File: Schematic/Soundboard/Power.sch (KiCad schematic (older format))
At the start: 34 parts, among them U1 STM32f429IIT6-units

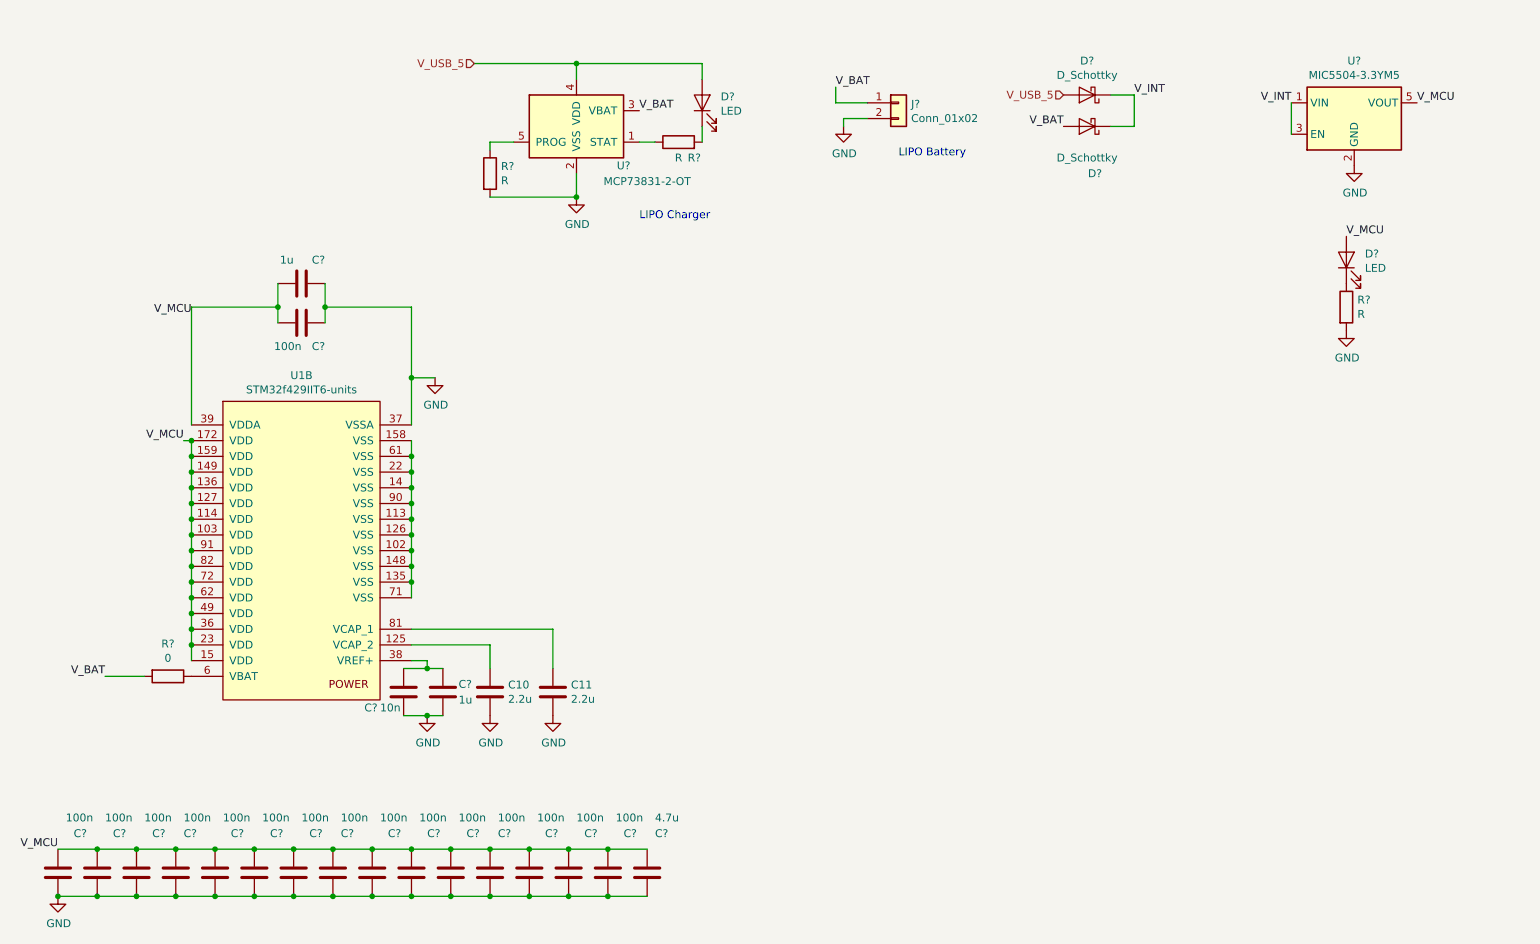
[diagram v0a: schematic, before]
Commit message: Complete part selection. Start connections
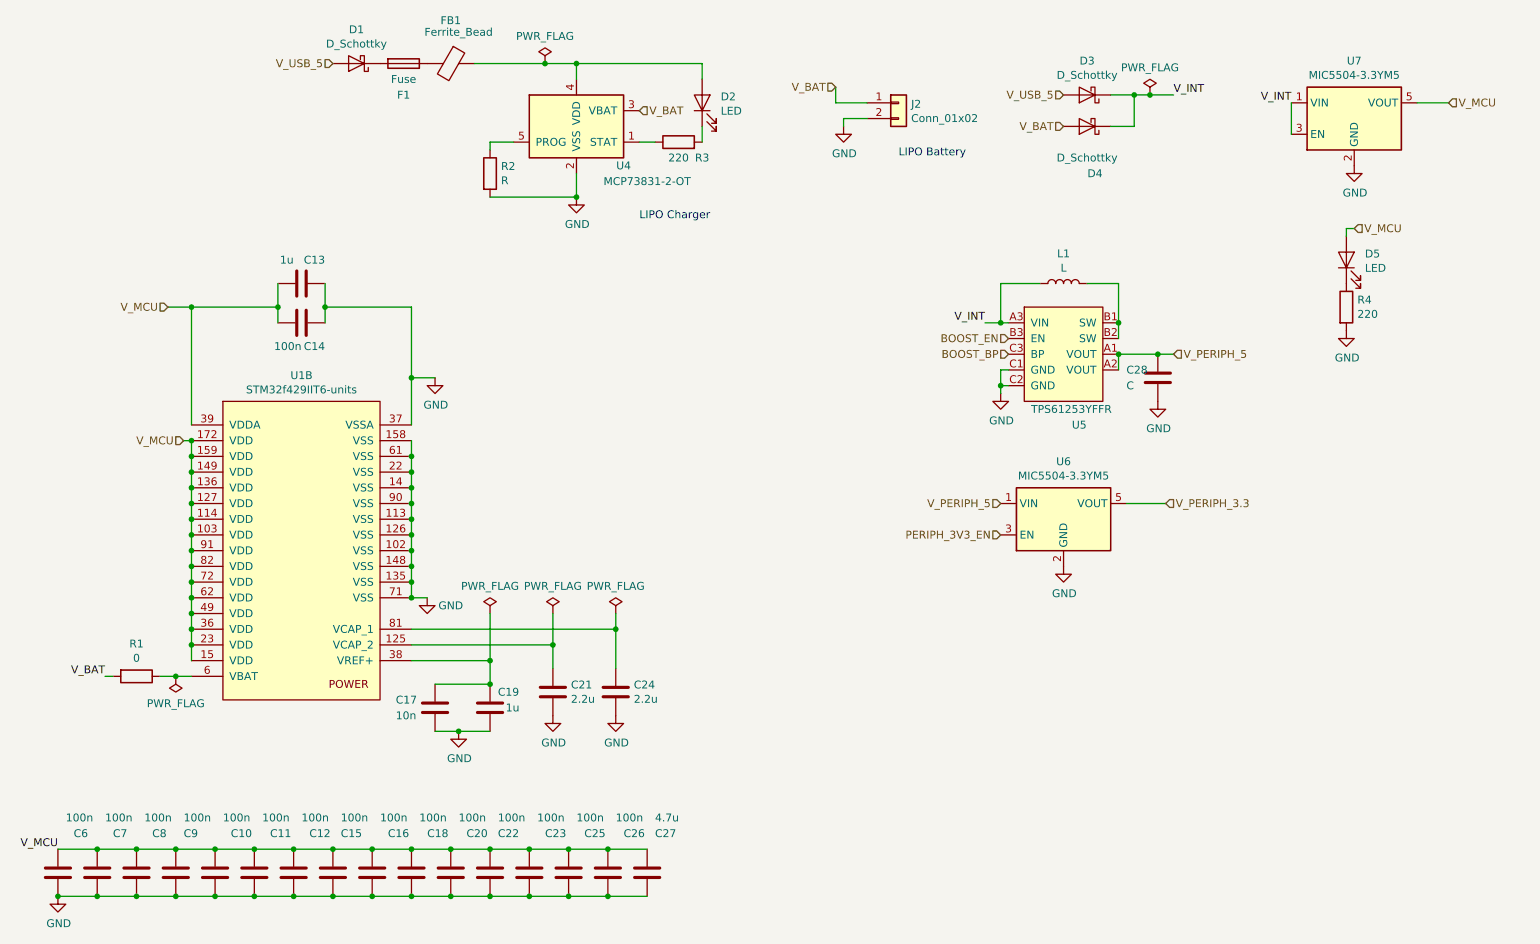
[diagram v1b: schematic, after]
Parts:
- added C28: C, Capacitor_SMD:C_0603_1608Metric_Pad1.05x0.95mm_HandSolder, symbol Device:C
- added D1: D_Schottky, Diode_SMD:D_0603_1608Metric_Pad1.05x0.95mm_HandSolder, symbol Device:D_Schottky
- added F1: Fuse, Fuse:Fuse_0603_1608Metric, symbol Device:Fuse
- added FB1: Ferrite_Bead, Inductor_SMD:L_0603_1608Metric, symbol Device:Ferrite_Bead
- added L1: L, Inductor_SMD:L_0603_1608Metric, symbol Device:L
- added U5: TPS61253YFFR, Package_BGA:Texas_MicroStar_Junior_BGA-113_7.0x7.0mm_Layout12x12_P0.5mm, symbol Soundboard:TPS61253YFFR
- added U6: MIC5504-3.3YM5, Package_TO_SOT_SMD:SOT-23-5, symbol Regulator_Linear:MIC5504-3.3YM5
- C10, C11, C12, C13, C14, C15, C16, C17, C18, C19, C20, C22, C23, C25, C26, C27, C6, C7, C8, C9: renamed from C?; footprint (none) -> Capacitor_SMD:C_0603_1608Metric_Pad1.05x0.95mm_HandSolder
- D2, D3, D4, D5: renamed from D?; footprint (none) -> Diode_SMD:D_0603_1608Metric_Pad1.05x0.95mm_HandSolder
- J2: renamed from J?; footprint (none) -> Connector_JST:JST_EH_B02B-EH-A_1x02_P2.50mm_Vertical
- R1, R2: renamed from R?; footprint (none) -> Resistor_SMD:R_0603_1608Metric_Pad1.05x0.95mm_HandSolder
- R3, R4: renamed from R?; value R -> 220; footprint (none) -> Resistor_SMD:R_0603_1608Metric_Pad1.05x0.95mm_HandSolder
- U1: footprint Package_QFP:LQFP-176_24x24mm_P0.5mm -> (none)
- gave numbers to parts that had none: 2
- renumbered C10 to C21, C11 to C24
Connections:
- net GND: now also U1.102 (VSS), U1.113 (VSS), U1.126 (VSS), U1.135 (VSS), U1.14 (VSS), U1.148 (VSS), U1.158 (VSS), U1.22 (VSS), U1.61 (VSS), U1.71 (VSS), U1.90 (VSS), C28.2, U5.C1 (GND), U5.C2 (GND), U6.2 (GND)
- net V_INT: now also L1.1, U5.A3 (VIN)
- net V_USB_5: now also D1.2 (A); no longer D2.2 (A), U4.4 (VDD)
- new net: L1.2, U5.B1 (SW), U5.B2 (SW)
- new net: D1.1 (K), F1.2
- new net: F1.1, FB1.2
- new net: D2.2 (A), FB1.1, U4.4 (VDD)
- new net BOOST_BP: U5.C3 (BP)
- new net BOOST_EN: U5.B3 (EN)
- new net PERIPH_3V3_EN: U6.3 (EN)
- new net V_PERIPH_3.3: U6.5 (VOUT)
- new net V_PERIPH_5: C28.1, U5.A1 (VOUT), U5.A2 (VOUT), U6.1 (VIN)
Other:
- moved on the sheet: C17, C19, C21, C24, R1

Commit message: Complete connections except for display to be chosen
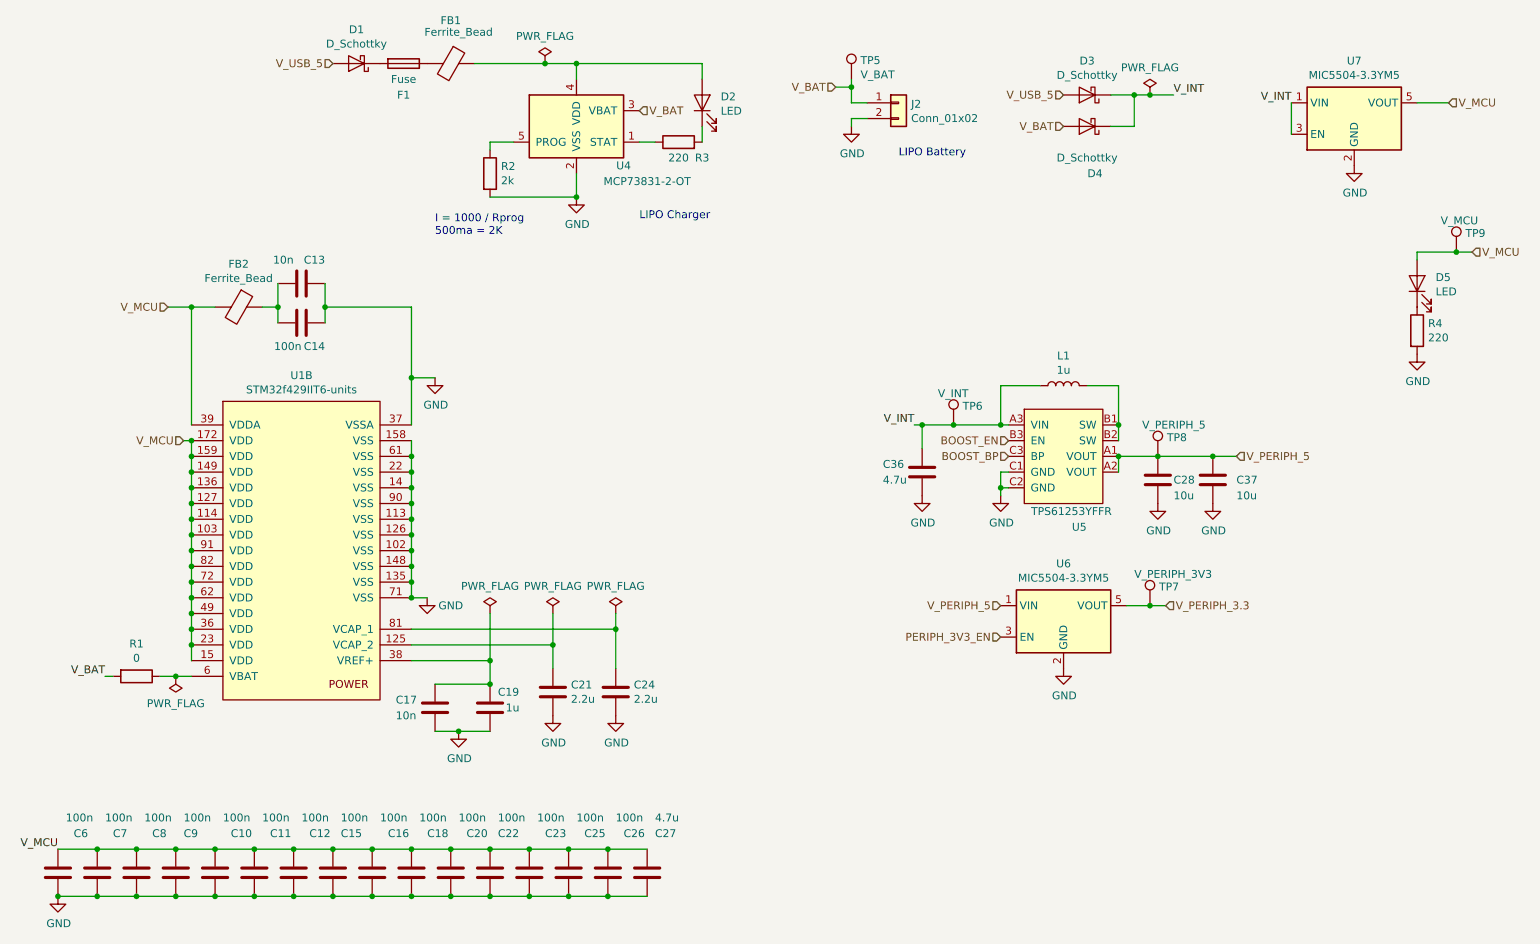
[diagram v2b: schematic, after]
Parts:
- added C36: 4.7u, symbol Device:C
- added C37: 10u, Capacitor_SMD:C_0603_1608Metric_Pad1.05x0.95mm_HandSolder, symbol Device:C
- added FB2: Ferrite_Bead, symbol Device:Ferrite_Bead
- added TP5: V_BAT, symbol Connector:TestPoint
- added TP6: V_INT, symbol Connector:TestPoint
- added TP7: V_PERIPH_3V3, symbol Connector:TestPoint
- added TP8: V_PERIPH_5, symbol Connector:TestPoint
- added TP9: V_MCU, symbol Connector:TestPoint
- C13: value 1u -> 10n
- C28: value C -> 10u
- L1: value L -> 1u
- R2: value R -> 2k
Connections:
- net GND: now also C36.2, C37.2
- net V_BAT: now also TP5.1
- net V_INT: now also C36.1, TP6.1
- net V_MCU: now also FB2.2, TP9.1; no longer C13.1, C14.1
- net V_PERIPH_3.3: now also TP7.1
- net V_PERIPH_5: now also C37.1, TP8.1
- new net: C13.1, C14.1, FB2.1
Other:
- note added: "I = 1000 / Rprog\n500ma = 2K\n"
- moved on the sheet: C28, D5, L1, R4, U5, U6

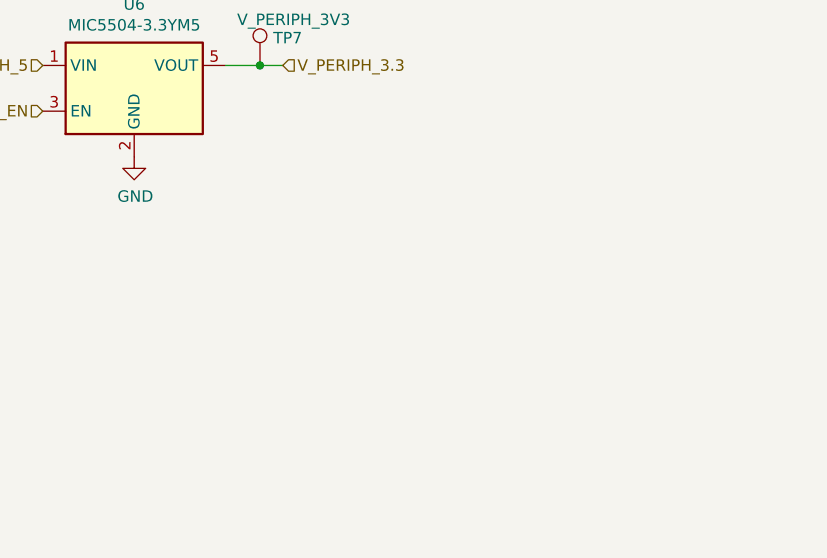
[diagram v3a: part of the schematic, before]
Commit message: Choose display. Complete schematic
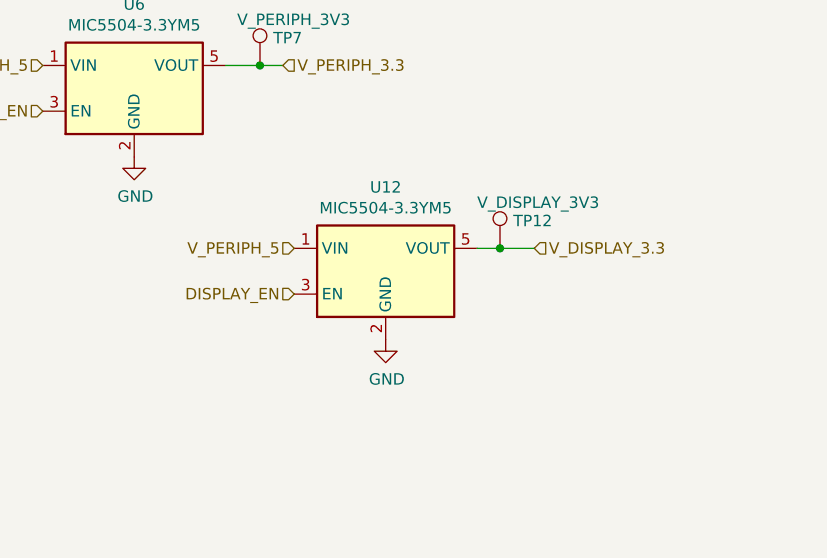
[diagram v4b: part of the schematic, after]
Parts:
- added TP12: V_DISPLAY_3V3, TestPoint:TestPoint_Pad_D2.0mm, symbol Connector:TestPoint
- added U12: MIC5504-3.3YM5, Package_TO_SOT_SMD:SOT-23-5, symbol Regulator_Linear:MIC5504-3.3YM5
- C36: footprint (none) -> Capacitor_SMD:C_0603_1608Metric_Pad1.05x0.95mm_HandSolder
- FB1: footprint Inductor_SMD:L_0603_1608Metric -> Inductor_SMD:L_0603_1608Metric_Pad1.05x0.95mm_HandSolder
- FB2: footprint (none) -> Inductor_SMD:L_0603_1608Metric_Pad1.05x0.95mm_HandSolder
- TP5, TP6, TP7, TP8, TP9: footprint (none) -> TestPoint:TestPoint_Pad_D2.0mm
- U1: footprint (none) -> Package_QFP:LQFP-176_24x24mm_P0.5mm
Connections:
- net GND: now also U12.2 (GND)
- net V_PERIPH_5: now also U12.1 (VIN)
- new net DISPLAY_EN: U12.3 (EN)
- new net V_DISPLAY_3.3: TP12.1, U12.5 (VOUT)
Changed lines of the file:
@@
 F 0 "FB1" V 3726 1500 50  0000 C CNN
 F 1 "Ferrite_Bead" V 3800 1550 50  0000 C CNN
-F 2 "Inductor_SMD:L_0603_1608Metric" V 3930 1500 50  0001 C CNN
+F 2 "Inductor_SMD:L_0603_1608Metric_Pad1.05x0.95mm_HandSolder" V 3930 1500 50  0001 C CNN
 F 3 "~" H 4000 1500 50  0001 C CNN
 	1    4000 1500
@@
 F 0 "U1" H 3050 3715 50  0000 C CNN
 F 1 "STM32f429IIT6-units" H 3050 3624 50  0000 C CNN
-F 2 "" H 3050 3600 50  0001 C CNN
+F 2 "Package_QFP:LQFP-176_24x24mm_P0.5mm" H 3050 3600 50  0001 C CNN
 F 3 "" H 3050 3600 50  0001 C CNN
 	2    3050 3600
@@
 F 0 "FB2" V 2376 3050 50  0000 C CNN
 F 1 "Ferrite_Bead" V 2467 3050 50  0000 C CNN
-F 2 "" V 2580 3050 50  0001 C CNN
+F 2 "Inductor_SMD:L_0603_1608Metric_Pad1.05x0.95mm_HandSolder" V 2580 3050 50  0001 C CNN
 F 3 "~" H 2650 3050 50  0001 C CNN
 	1    2650 3050
@@
 F 0 "C36" H 6750 4150 50  0000 L CNN
 F 1 "4.7u" H 6750 4050 50  0000 L CNN
-F 2 "" H 7038 3950 50  0001 C CNN
+F 2 "Capacitor_SMD:C_0603_1608Metric_Pad1.05x0.95mm_HandSolder" H 7038 3950 50  0001 C CNN
 F 3 "~" H 7000 4100 50  0001 C CNN
 	1    7000 4100
@@
 F 0 "TP5" H 6608 1720 50  0000 L CNN
 F 1 "V_BAT" H 6608 1629 50  0000 L CNN
-F 2 "" H 6750 1600 50  0001 C CNN
+F 2 "TestPoint:TestPoint_Pad_D2.0mm" H 6750 1600 50  0001 C CNN
 F 3 "~" H 6750 1600 50  0001 C CNN
 	1    6550 1600
@@
 F 0 "TP6" H 7258 3920 50  0000 L CNN
 F 1 "V_INT" H 7100 4000 50  0000 L CNN
-F 2 "" H 7400 3800 50  0001 C CNN
+F 2 "TestPoint:TestPoint_Pad_D2.0mm" H 7400 3800 50  0001 C CNN
 F 3 "~" H 7400 3800 50  0001 C CNN
 	1    7200 3800
@@
 F 0 "TP9" H 10458 2820 50  0000 L CNN
 F 1 "V_MCU" H 10300 2900 50  0000 L CNN
-F 2 "" H 10600 2700 50  0001 C CNN
+F 2 "TestPoint:TestPoint_Pad_D2.0mm" H 10600 2700 50  0001 C CNN
 F 3 "~" H 10600 2700 50  0001 C CNN
 	1    10400 2700
@@
 F 0 "TP8" H 8558 4120 50  0000 L CNN
 F 1 "V_PERIPH_5" H 8400 4200 50  0000 L CNN
-F 2 "" H 8700 4000 50  0001 C CNN
+F 2 "TestPoint:TestPoint_Pad_D2.0mm" H 8700 4000 50  0001 C CNN
 F 3 "~" H 8700 4000 50  0001 C CNN
 	1    8500 4000
@@
 F 0 "TP7" H 8508 5070 50  0000 L CNN
 F 1 "V_PERIPH_3V3" H 8350 5150 50  0000 L CNN
-F 2 "" H 8650 4950 50  0001 C CNN
+F 2 "TestPoint:TestPoint_Pad_D2.0mm" H 8650 4950 50  0001 C CNN
 F 3 "~" H 8650 4950 50  0001 C CNN
 	1    8450 4950
@@
 Wire Wire Line
 	8450 4950 8550 4950
+$Comp
+L Regulator_Linear:MIC5504-3.3YM5 U12
+U 1 1 5F67A1CD
+P 9000 5850
+F 0 "U12" H 9000 6217 50  0000 C CNN
+F 1 "MIC5504-3.3YM5" H 9000 6126 50  0000 C CNN
+F 2 "Package_TO_SOT_SMD:SOT-23-5" H 9000 5450 50  0001 C CNN
+F 3 "http://ww1.microchip.com/downloads/en/DeviceDoc/MIC550X.pdf" H 8750 6100 50  0001 C CNN
+	1    9000 5850
+	1    0    0    -1
+$EndComp
+$Comp
+L power:GND #PWR050
+U 1 1 5F67A1D3
+P 9000 6150
+F 0 "#PWR050" H 9000 5900 50  0001 C CNN
+F 1 "GND" H 9005 5977 50  0000 C CNN
+F 2 "" H 9000 6150 50  0001 C CNN
+F 3 "" H 9000 6150 50  0001 C CNN
+	1    9000 6150
+	1    0    0    -1
+$EndComp
+Text HLabel 9650 5750 2    50   Input ~ 0
+V_DISPLAY_3.3
+Text HLabel 8600 5750 0    50   Input ~ 0
+V_PERIPH_5
+Text HLabel 8600 5950 0    50   Input ~ 0
+DISPLAY_EN
+Wire Wire Line
+	9400 5750 9500 5750
+$Comp
+L Connector:TestPoint TP12
+U 1 1 5F6DB3A6
+P 9500 5750
+F 0 "TP12" H 9558 5870 50  0000 L CNN
+F 1 "V_DISPLAY_3V3" H 9400 5950 50  0000 L CNN
+F 2 "TestPoint:TestPoint_Pad_D2.0mm" H 9700 5750 50  0001 C CNN
+F 3 "~" H 9700 5750 50  0001 C CNN
+	1    9500 5750
+	1    0    0    -1
+$EndComp
+Connection ~ 9500 5750
+Wire Wire Line
+	9500 5750 9650 5750
 $EndSCHEMATC
